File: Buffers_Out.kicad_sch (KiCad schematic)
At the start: 37 parts, among them U6 NE5532, U7 NE5532, X1 PEDAL_COMBO_TOP

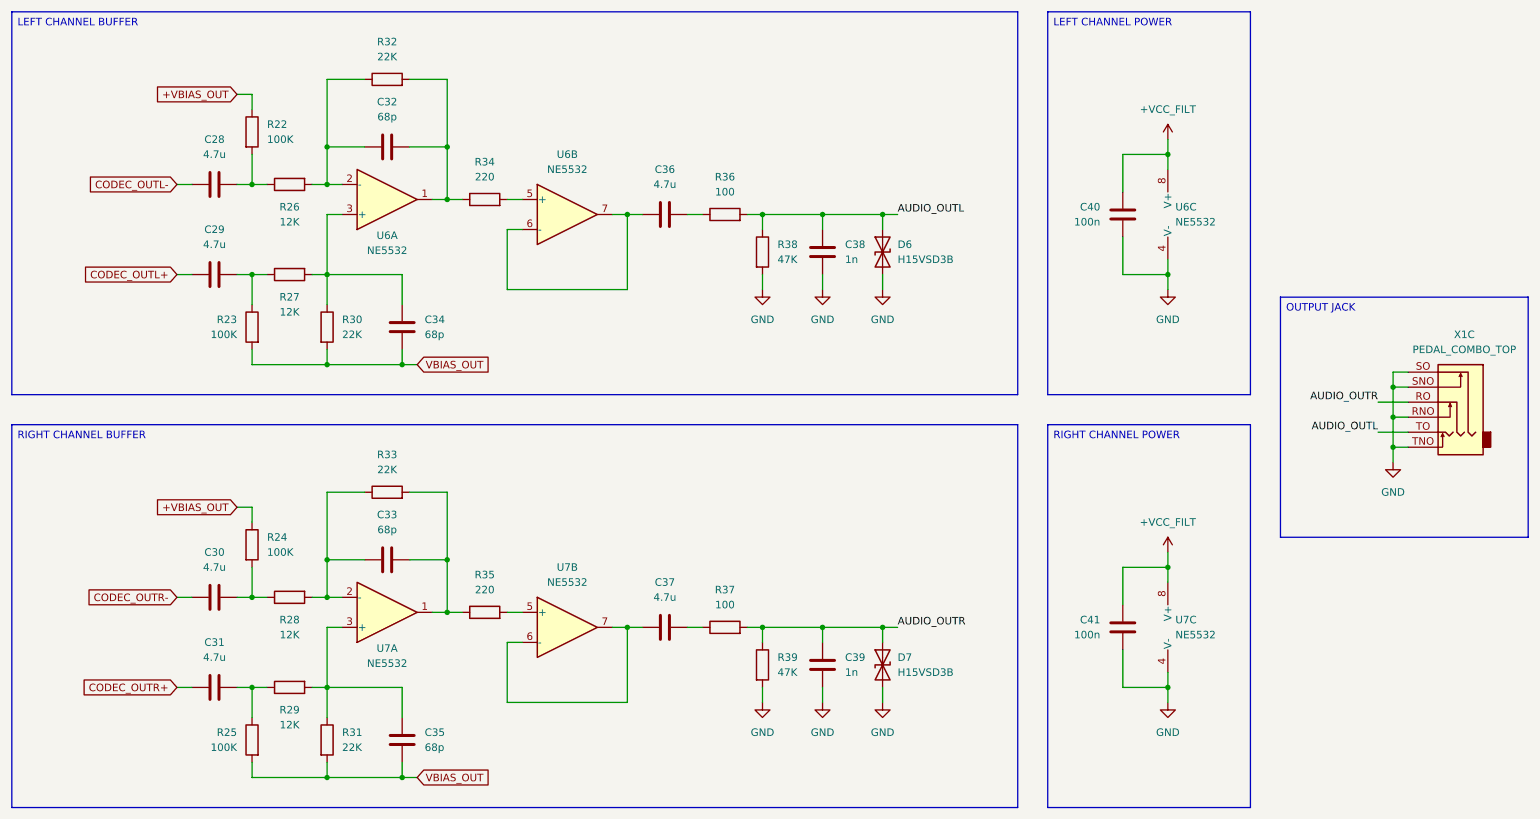
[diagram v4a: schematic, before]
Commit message: RP2350 layout
Updated the layout for the RP2350.
Added board headers.
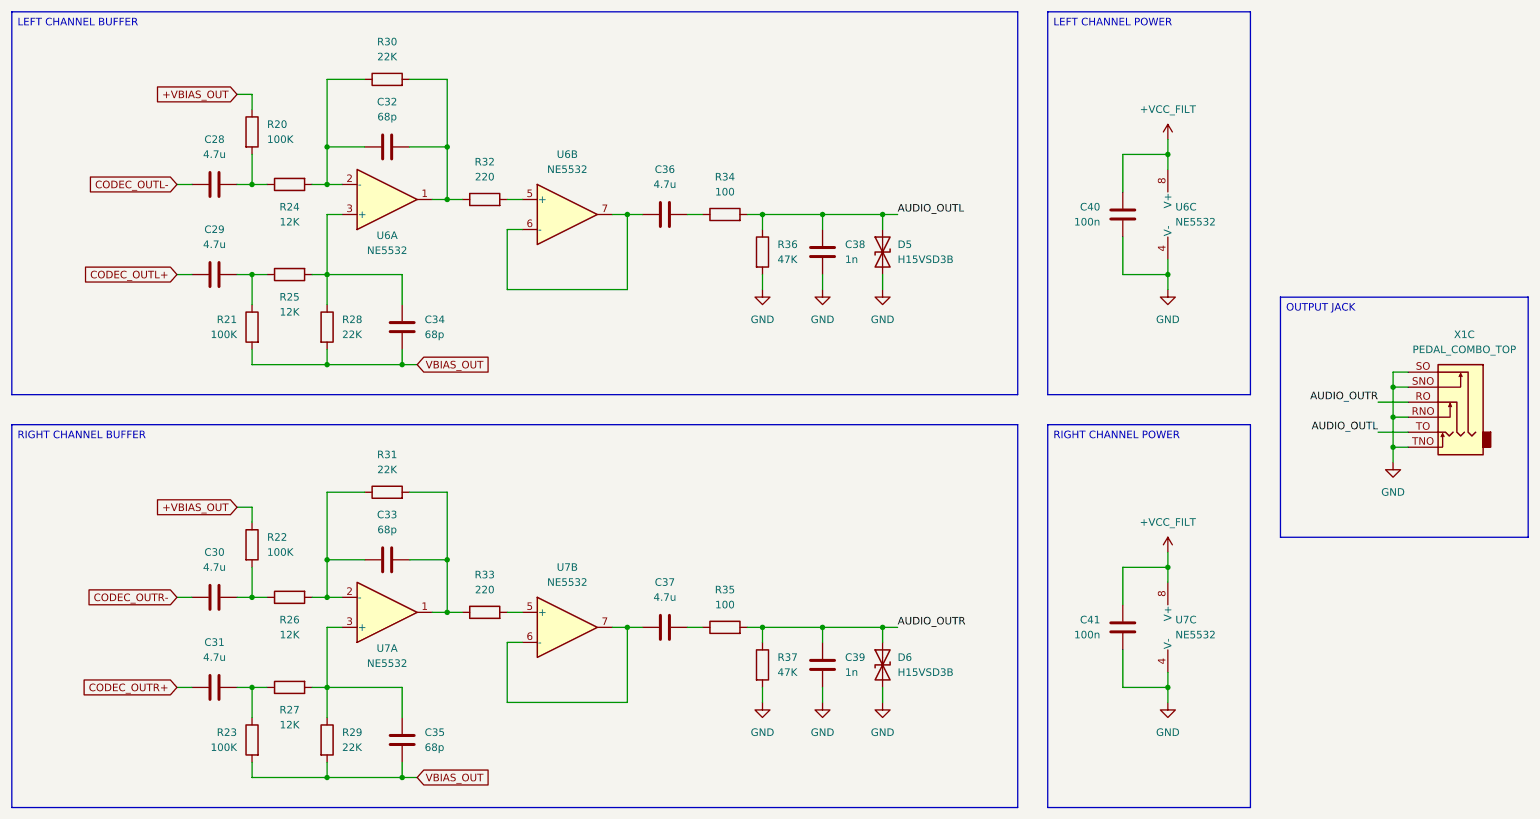
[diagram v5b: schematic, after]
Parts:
- renumbered D6 to D5, D7 to D6, R22 to R20, R23 to R21, R24 to R22, R25 to R23, R26 to R24, R27 to R25, R28 to R26, R29 to R27, R30 to R28, R31 to R29, R32 to R30, R33 to R31, R34 to R32, R35 to R33, R36 to R34, R37 to R35, R38 to R36, R39 to R37
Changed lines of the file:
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@@
 		(on_board yes)
 		(dnp no)
-		(property "Reference" "D7"
+		(property "Reference" "D6"
 			(at 171.45 130.8101 90)
 			(effects
@@
 			(project "SimpleCodec"
 				(path "/4cbf131b-42e8-4a05-beea-68c6d66cdb1a/f30b69e3-f4a5-44b3-bff9-cd489323ac3e"
-					(reference "D7")
+					(reference "D6")
 					(unit 1)
 				)
@@
 		(on_board yes)
 		(dnp no)
-		(property "Reference" "R26"
+		(property "Reference" "R24"
 			(at 68.58 54.61 90)
 			(effects
@@
 			(project "SimpleCodec"
 				(path "/4cbf131b-42e8-4a05-beea-68c6d66cdb1a/f30b69e3-f4a5-44b3-bff9-cd489323ac3e"
-					(reference "R26")
+					(reference "R24")
 					(unit 1)
 				)
@@
 		(dnp no)
 		(fields_autoplaced yes)
-		(property "Reference" "R34"
+		(property "Reference" "R32"
 			(at 101.6 46.99 90)
 			(effects
@@
 			(project "SimpleCodec"
 				(path "/4cbf131b-42e8-4a05-beea-68c6d66cdb1a/f30b69e3-f4a5-44b3-bff9-cd489323ac3e"
-					(reference "R34")
+					(reference "R32")
 					(unit 1)
 				)
@@
 		(on_board yes)
 		(dnp no)
-		(property "Reference" "R30"
+		(property "Reference" "R28"
 			(at 77.47 73.6599 0)
 			(effects
@@
 			(project "SimpleCodec"
 				(path "/4cbf131b-42e8-4a05-beea-68c6d66cdb1a/f30b69e3-f4a5-44b3-bff9-cd489323ac3e"
-					(reference "R30")
+					(reference "R28")
 					(unit 1)
 				)
@@
 		(dnp no)
 		(fields_autoplaced yes)
-		(property "Reference" "R35"
+		(property "Reference" "R33"
 			(at 101.6 116.84 90)
 			(effects
@@
 			(project "SimpleCodec"
 				(path "/4cbf131b-42e8-4a05-beea-68c6d66cdb1a/f30b69e3-f4a5-44b3-bff9-cd489323ac3e"
-					(reference "R35")
+					(reference "R33")
 					(unit 1)
 				)
@@
 		(on_board yes)
 		(dnp no)
-		(property "Reference" "D6"
+		(property "Reference" "D5"
 			(at 171.45 60.9601 90)
 			(effects
@@
 			(project "SimpleCodec"
 				(path "/4cbf131b-42e8-4a05-beea-68c6d66cdb1a/f30b69e3-f4a5-44b3-bff9-cd489323ac3e"
-					(reference "D6")
+					(reference "D5")
 					(unit 1)
 				)
@@
 		(on_board yes)
 		(dnp no)
-		(property "Reference" "R25"
+		(property "Reference" "R23"
 			(at 59.69 143.5099 0)
 			(effects
@@
 			(project "SimpleCodec"
 				(path "/4cbf131b-42e8-4a05-beea-68c6d66cdb1a/f30b69e3-f4a5-44b3-bff9-cd489323ac3e"
-					(reference "R25")
+					(reference "R23")
 					(unit 1)
 				)
@@
 		(dnp no)
 		(fields_autoplaced yes)
-		(property "Reference" "R32"
+		(property "Reference" "R30"
 			(at 85.09 26.67 90)
 			(effects
@@
 			(project "SimpleCodec"
 				(path "/4cbf131b-42e8-4a05-beea-68c6d66cdb1a/f30b69e3-f4a5-44b3-bff9-cd489323ac3e"
-					(reference "R32")
+					(reference "R30")
 					(unit 1)
 				)
@@
 		(on_board yes)
 		(dnp no)
-		(property "Reference" "R27"
+		(property "Reference" "R25"
 			(at 68.58 69.85 90)
 			(effects
@@
 			(project "SimpleCodec"
 				(path "/4cbf131b-42e8-4a05-beea-68c6d66cdb1a/f30b69e3-f4a5-44b3-bff9-cd489323ac3e"
-					(reference "R27")
+					(reference "R25")
 					(unit 1)
 				)
@@
 		(on_board yes)
 		(dnp no)
-		(property "Reference" "R24"
+		(property "Reference" "R22"
 			(at 64.77 110.4899 0)
 			(effects
@@
 			(project "SimpleCodec"
 				(path "/4cbf131b-42e8-4a05-beea-68c6d66cdb1a/f30b69e3-f4a5-44b3-bff9-cd489323ac3e"
-					(reference "R24")
+					(reference "R22")
 					(unit 1)
 				)
@@
 		(on_board yes)
 		(dnp no)
-		(property "Reference" "R22"
+		(property "Reference" "R20"
 			(at 64.77 40.6399 0)
 			(effects
@@
 			(project "SimpleCodec"
 				(path "/4cbf131b-42e8-4a05-beea-68c6d66cdb1a/f30b69e3-f4a5-44b3-bff9-cd489323ac3e"
-					(reference "R22")
+					(reference "R20")
 					(unit 1)
 				)
@@
 		(dnp no)
 		(fields_autoplaced yes)
-		(property "Reference" "R33"
+		(property "Reference" "R31"
 			(at 85.09 96.52 90)
 			(effects
@@
 			(project "SimpleCodec"
 				(path "/4cbf131b-42e8-4a05-beea-68c6d66cdb1a/f30b69e3-f4a5-44b3-bff9-cd489323ac3e"
-					(reference "R33")
+					(reference "R31")
 					(unit 1)
 				)
@@
 		(dnp no)
 		(fields_autoplaced yes)
-		(property "Reference" "R39"
+		(property "Reference" "R37"
 			(at 151.13 130.8099 0)
 			(effects
@@
 			(project "SimpleCodec"
 				(path "/4cbf131b-42e8-4a05-beea-68c6d66cdb1a/f30b69e3-f4a5-44b3-bff9-cd489323ac3e"
-					(reference "R39")
+					(reference "R37")
 					(unit 1)
 				)
@@
 		(on_board yes)
 		(dnp no)
-		(property "Reference" "R23"
+		(property "Reference" "R21"
 			(at 59.69 73.6599 0)
 			(effects
@@
 			(project "SimpleCodec"
 				(path "/4cbf131b-42e8-4a05-beea-68c6d66cdb1a/f30b69e3-f4a5-44b3-bff9-cd489323ac3e"
-					(reference "R23")
+					(reference "R21")
 					(unit 1)
 				)
@@
 		(dnp no)
 		(fields_autoplaced yes)
-		(property "Reference" "R36"
+		(property "Reference" "R34"
 			(at 142.24 49.53 90)
 			(effects
@@
 			(project "SimpleCodec"
 				(path "/4cbf131b-42e8-4a05-beea-68c6d66cdb1a/f30b69e3-f4a5-44b3-bff9-cd489323ac3e"
-					(reference "R36")
+					(reference "R34")
 					(unit 1)
 				)
@@
 		(dnp no)
 		(fields_autoplaced yes)
-		(property "Reference" "R37"
+		(property "Reference" "R35"
 			(at 142.24 119.38 90)
 			(effects
@@
 			(project "SimpleCodec"
 				(path "/4cbf131b-42e8-4a05-beea-68c6d66cdb1a/f30b69e3-f4a5-44b3-bff9-cd489323ac3e"
-					(reference "R37")
+					(reference "R35")
 					(unit 1)
 				)
@@
 		(on_board yes)
 		(dnp no)
-		(property "Reference" "R29"
+		(property "Reference" "R27"
 			(at 68.58 139.7 90)
 			(effects
@@
 			(project "SimpleCodec"
 				(path "/4cbf131b-42e8-4a05-beea-68c6d66cdb1a/f30b69e3-f4a5-44b3-bff9-cd489323ac3e"
-					(reference "R29")
+					(reference "R27")
 					(unit 1)
 				)
@@
 		(on_board yes)
 		(dnp no)
-		(property "Reference" "R31"
+		(property "Reference" "R29"
 			(at 77.47 143.5099 0)
 			(effects
@@
 			(project "SimpleCodec"
 				(path "/4cbf131b-42e8-4a05-beea-68c6d66cdb1a/f30b69e3-f4a5-44b3-bff9-cd489323ac3e"
-					(reference "R31")
+					(reference "R29")
 					(unit 1)
 				)
@@
 		(on_board yes)
 		(dnp no)
-		(property "Reference" "R28"
+		(property "Reference" "R26"
 			(at 68.58 124.46 90)
 			(effects
@@
 			(project "SimpleCodec"
 				(path "/4cbf131b-42e8-4a05-beea-68c6d66cdb1a/f30b69e3-f4a5-44b3-bff9-cd489323ac3e"
-					(reference "R28")
+					(reference "R26")
 					(unit 1)
 				)
@@
 		(dnp no)
 		(fields_autoplaced yes)
-		(property "Reference" "R38"
+		(property "Reference" "R36"
 			(at 151.13 60.9599 0)
 			(effects
@@
 			(project "SimpleCodec"
 				(path "/4cbf131b-42e8-4a05-beea-68c6d66cdb1a/f30b69e3-f4a5-44b3-bff9-cd489323ac3e"
-					(reference "R38")
+					(reference "R36")
 					(unit 1)
 				)
